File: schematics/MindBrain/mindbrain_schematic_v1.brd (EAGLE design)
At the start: 92.4 x 49.5 mm, 47 parts, among them CON1 POWER, IC1 TL084P, IC2 TL084P

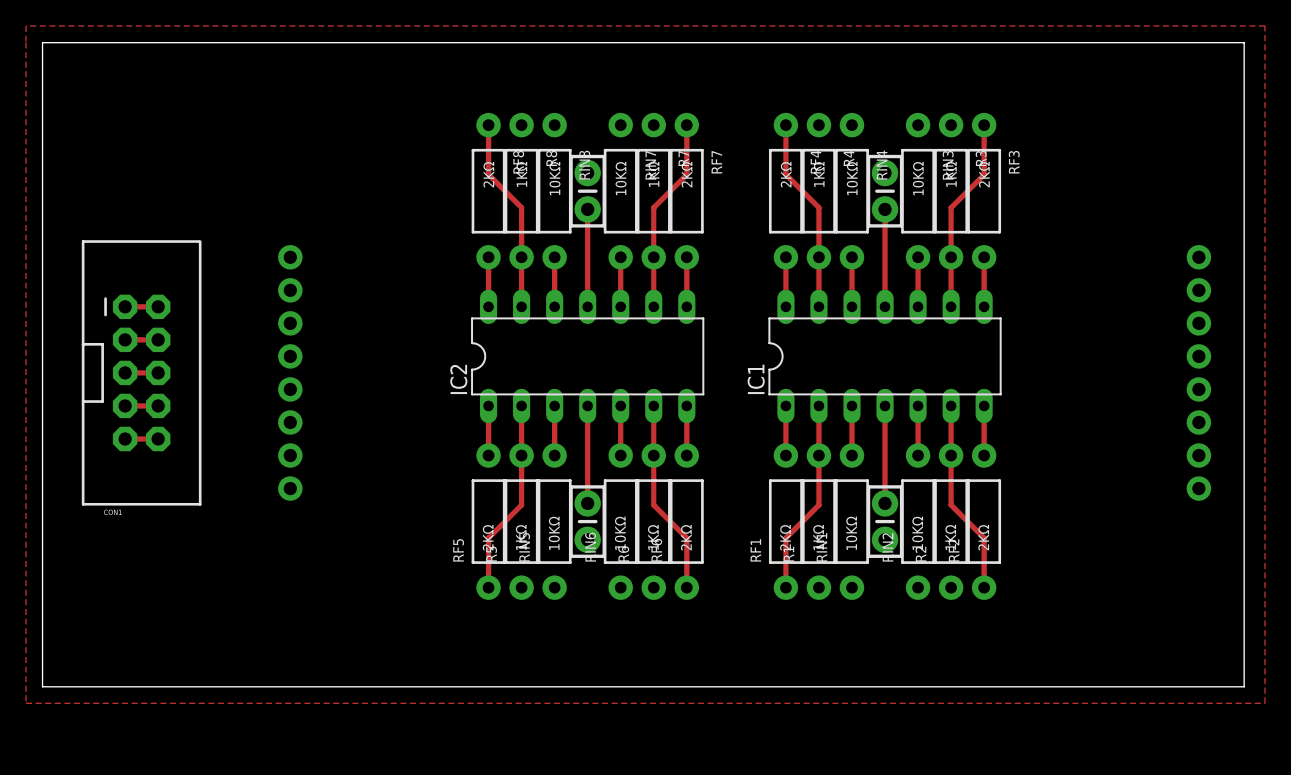
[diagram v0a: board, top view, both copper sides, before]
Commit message: not so sure about ground pour. Going back to airwired grounds for now
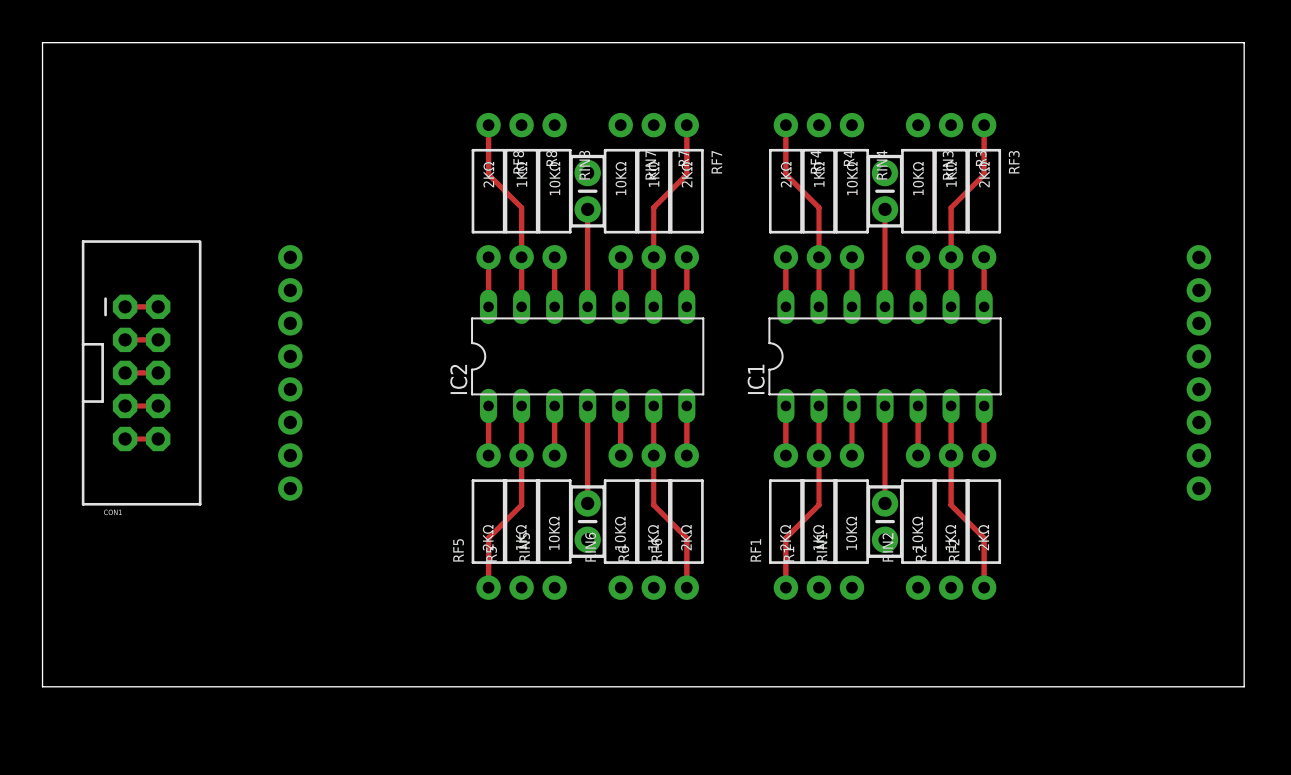
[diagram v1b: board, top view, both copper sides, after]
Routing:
- removed copper zone on layer 1, net GND
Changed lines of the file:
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@@
 <contactref element="RIN1" pad="P$2"/>
 <contactref element="IC1" pad="3"/>
+<wire x1="19.05" y1="15.24" x2="62.23" y2="17.78" width="0" layer="19" extent="1-1"/>
 <wire x1="62.23" y1="21.59" x2="62.23" y2="17.78" width="0.4064" layer="1"/>
-<wire x1="19.05" y1="15.24" x2="62.23" y2="17.78" width="0" layer="19" extent="1-1"/>
 </signal>
 <signal name="GND">
@@
 <wire x1="6.35" y1="26.67" x2="8.89" y2="26.67" width="0.4064" layer="1"/>
 <wire x1="6.35" y1="24.13" x2="8.89" y2="24.13" width="0.4064" layer="1"/>
-<polygon width="0.4064" layer="1">
-<vertex x="-1.27" y="-1.27"/>
-<vertex x="93.98" y="-1.27"/>
-<vertex x="93.98" y="50.8"/>
-<vertex x="-1.27" y="50.8"/>
-<vertex x="-1.27" y="49.53"/>
-</polygon>
+<wire x1="67.31" y1="43.18" x2="69.85" y2="43.18" width="0" layer="19" extent="1-1"/>
+<wire x1="64.77" y1="39.497" x2="67.31" y2="43.18" width="0" layer="19" extent="1-1"/>
+<wire x1="62.23" y1="43.18" x2="64.77" y2="39.497" width="0" layer="19" extent="1-1"/>
+<wire x1="59.69" y1="43.18" x2="62.23" y2="43.18" width="0" layer="19" extent="1-1"/>
+<wire x1="46.99" y1="43.18" x2="59.69" y2="43.18" width="0" layer="19" extent="1-1"/>
+<wire x1="44.45" y1="43.18" x2="46.99" y2="43.18" width="0" layer="19" extent="1-1"/>
+<wire x1="41.91" y1="39.497" x2="44.45" y2="43.18" width="0" layer="19" extent="1-1"/>
+<wire x1="39.37" y1="43.18" x2="41.91" y2="39.497" width="0" layer="19" extent="1-1"/>
+<wire x1="36.83" y1="43.18" x2="39.37" y2="43.18" width="0" layer="19" extent="1-1"/>
+<wire x1="64.77" y1="11.303" x2="64.77" y2="39.497" width="0" layer="19" extent="1-1"/>
+<wire x1="67.31" y1="7.62" x2="64.77" y2="11.303" width="0" layer="19" extent="1-1"/>
+<wire x1="69.85" y1="7.62" x2="67.31" y2="7.62" width="0" layer="19" extent="1-1"/>
+<wire x1="62.23" y1="7.62" x2="64.77" y2="11.303" width="0" layer="19" extent="1-1"/>
+<wire x1="59.69" y1="7.62" x2="62.23" y2="7.62" width="0" layer="19" extent="1-1"/>
+<wire x1="46.99" y1="7.62" x2="59.69" y2="7.62" width="0" layer="19" extent="1-1"/>
+<wire x1="44.45" y1="7.62" x2="46.99" y2="7.62" width="0" layer="19" extent="1-1"/>
+<wire x1="41.91" y1="11.303" x2="44.45" y2="7.62" width="0" layer="19" extent="1-1"/>
+<wire x1="39.37" y1="7.62" x2="41.91" y2="11.303" width="0" layer="19" extent="1-1"/>
+<wire x1="36.83" y1="7.62" x2="39.37" y2="7.62" width="0" layer="19" extent="1-1"/>
+<wire x1="8.89" y1="21.59" x2="36.83" y2="7.62" width="0" layer="19" extent="1-1"/>
+<wire x1="8.89" y1="24.13" x2="8.89" y2="21.59" width="0" layer="19" extent="1-1"/>
+<wire x1="8.89" y1="26.67" x2="8.89" y2="24.13" width="0" layer="19" extent="1-1"/>
 </signal>
 <signal name="N$2">
@@
 <contactref element="RF1" pad="P$2"/>
 <contactref element="IC1" pad="1"/>
+<wire x1="57.15" y1="17.78" x2="88.9" y2="15.24" width="0" layer="19" extent="1-1"/>
 <wire x1="57.15" y1="21.59" x2="57.15" y2="17.78" width="0.4064" layer="1"/>
-<wire x1="57.15" y1="17.78" x2="88.9" y2="15.24" width="0" layer="19" extent="1-1"/>
 </signal>
 <signal name="N$3">
@@
 <contactref element="RIN2" pad="P$2"/>
 <contactref element="IC1" pad="5"/>
+<wire x1="19.05" y1="17.78" x2="67.31" y2="17.78" width="0" layer="19" extent="1-1"/>
 <wire x1="67.31" y1="21.59" x2="67.31" y2="17.78" width="0.4064" layer="1"/>
-<wire x1="19.05" y1="17.78" x2="67.31" y2="17.78" width="0" layer="19" extent="1-1"/>
 </signal>
 <signal name="N$5">
@@
 <contactref element="IC1" pad="7"/>
 <wire x1="72.39" y1="21.59" x2="72.39" y2="17.78" width="0.4064" layer="1"/>
-<wire x1="72.39" y1="17.78" x2="88.9" y2="17.78" width="0" layer="19" extent="1-1"/>
+<wire x1="88.9" y1="17.78" x2="72.39" y2="17.78" width="0" layer="19" extent="1-16"/>
 </signal>
 <signal name="N$6">
@@
 <contactref element="RIN3" pad="P$2"/>
 <contactref element="IC1" pad="10"/>
+<wire x1="19.05" y1="20.32" x2="67.31" y2="33.02" width="0" layer="19" extent="1-1"/>
 <wire x1="67.31" y1="29.21" x2="67.31" y2="33.02" width="0.4064" layer="1"/>
-<wire x1="19.05" y1="20.32" x2="67.31" y2="29.21" width="0" layer="19" extent="1-1"/>
 </signal>
 <signal name="N$8">
@@
 <contactref element="IC1" pad="8"/>
 <wire x1="72.39" y1="29.21" x2="72.39" y2="33.02" width="0.4064" layer="1"/>
-<wire x1="72.39" y1="29.21" x2="88.9" y2="20.32" width="0" layer="19" extent="1-1"/>
+<wire x1="72.39" y1="33.02" x2="88.9" y2="20.32" width="0" layer="19" extent="1-16"/>
 </signal>
 <signal name="N$9">
@@
 <contactref element="RIN4" pad="P$2"/>
 <contactref element="IC1" pad="12"/>
+<wire x1="62.23" y1="33.02" x2="19.05" y2="22.86" width="0" layer="19" extent="1-1"/>
 <wire x1="62.23" y1="29.21" x2="62.23" y2="33.02" width="0.4064" layer="1"/>
-<wire x1="19.05" y1="22.86" x2="62.23" y2="29.21" width="0" layer="19" extent="1-1"/>
 </signal>
 <signal name="N$11">
@@
 <contactref element="RF4" pad="P$2"/>
 <contactref element="IC1" pad="14"/>
+<wire x1="57.15" y1="33.02" x2="88.9" y2="22.86" width="0" layer="19" extent="1-1"/>
 <wire x1="57.15" y1="29.21" x2="57.15" y2="33.02" width="0.4064" layer="1"/>
-<wire x1="57.15" y1="29.21" x2="88.9" y2="22.86" width="0" layer="19" extent="1-1"/>
 </signal>
 <signal name="N$12">
@@
 <contactref element="RIN5" pad="P$2"/>
 <contactref element="IC2" pad="3"/>
+<wire x1="19.05" y1="25.4" x2="39.37" y2="17.78" width="0" layer="19" extent="1-1"/>
 <wire x1="39.37" y1="21.59" x2="39.37" y2="17.78" width="0.4064" layer="1"/>
-<wire x1="19.05" y1="25.4" x2="39.37" y2="21.59" width="0" layer="19" extent="1-1"/>
 </signal>
 <signal name="N$14">
@@
 <contactref element="RF5" pad="P$2"/>
 <contactref element="IC2" pad="1"/>
+<wire x1="88.9" y1="25.4" x2="34.29" y2="17.78" width="0" layer="19" extent="1-1"/>
 <wire x1="34.29" y1="21.59" x2="34.29" y2="17.78" width="0.4064" layer="1"/>
-<wire x1="34.29" y1="21.59" x2="88.9" y2="25.4" width="0" layer="19" extent="1-1"/>
 </signal>
 <signal name="N$15">
@@
 <contactref element="RIN6" pad="P$2"/>
 <contactref element="IC2" pad="5"/>
+<wire x1="19.05" y1="27.94" x2="44.45" y2="17.78" width="0" layer="19" extent="1-1"/>
 <wire x1="44.45" y1="17.78" x2="44.45" y2="21.59" width="0.4064" layer="1"/>
-<wire x1="19.05" y1="27.94" x2="44.45" y2="21.59" width="0" layer="19" extent="1-1"/>
 </signal>
 <signal name="N$17">
@@
 <contactref element="RF6" pad="P$2"/>
 <contactref element="IC2" pad="7"/>
+<wire x1="88.9" y1="27.94" x2="49.53" y2="17.78" width="0" layer="19" extent="1-1"/>
 <wire x1="49.53" y1="21.59" x2="49.53" y2="17.78" width="0.4064" layer="1"/>
-<wire x1="49.53" y1="21.59" x2="88.9" y2="27.94" width="0" layer="19" extent="1-1"/>
 </signal>
 <signal name="N$18">
@@
 <contactref element="RIN7" pad="P$2"/>
 <contactref element="IC2" pad="10"/>
+<wire x1="44.45" y1="33.02" x2="19.05" y2="30.48" width="0" layer="19" extent="1-1"/>
 <wire x1="44.45" y1="33.02" x2="44.45" y2="29.21" width="0.4064" layer="1"/>
-<wire x1="19.05" y1="30.48" x2="44.45" y2="29.21" width="0" layer="19" extent="1-1"/>
 </signal>
 <signal name="N$20">
@@
 <contactref element="RF7" pad="P$2"/>
 <contactref element="IC2" pad="8"/>
+<wire x1="88.9" y1="30.48" x2="49.53" y2="33.02" width="0" layer="19" extent="1-1"/>
 <wire x1="49.53" y1="29.21" x2="49.53" y2="33.02" width="0.4064" layer="1"/>
-<wire x1="49.53" y1="29.21" x2="88.9" y2="30.48" width="0" layer="19" extent="1-1"/>
 </signal>
 <signal name="N$21">
@@
 <contactref element="RIN8" pad="P$2"/>
 <contactref element="IC2" pad="12"/>
+<wire x1="19.05" y1="33.02" x2="39.37" y2="33.02" width="0" layer="19" extent="1-1"/>
 <wire x1="39.37" y1="29.21" x2="39.37" y2="33.02" width="0.4064" layer="1"/>
-<wire x1="19.05" y1="33.02" x2="39.37" y2="33.02" width="0" layer="19" extent="1-1"/>
 </signal>
 <signal name="N$23">
@@
 <contactref element="C2" pad="1"/>
 <contactref element="C4" pad="1"/>
+<wire x1="41.91" y1="29.21" x2="64.77" y2="29.21" width="0" layer="19" extent="1-1"/>
 <wire x1="64.77" y1="36.703" x2="64.77" y2="29.21" width="0.4064" layer="1"/>
 <wire x1="41.91" y1="36.703" x2="41.91" y2="29.21" width="0.4064" layer="1"/>
+<wire x1="8.89" y1="29.21" x2="41.91" y2="29.21" width="0" layer="19" extent="1-1"/>
 <wire x1="6.35" y1="29.21" x2="8.89" y2="29.21" width="0.4064" layer="1"/>
-<wire x1="41.91" y1="36.703" x2="64.77" y2="36.703" width="0" layer="19" extent="1-1"/>
-<wire x1="8.89" y1="29.21" x2="41.91" y2="29.21" width="0" layer="19" extent="1-1"/>
 </signal>
 <signal name="N$25">
@@
 <contactref element="C3" pad="1"/>
 <contactref element="CON1" pad="10"/>
+<wire x1="41.91" y1="21.59" x2="64.77" y2="21.59" width="0" layer="19" extent="1-1"/>
+<wire x1="8.89" y1="19.05" x2="41.91" y2="21.59" width="0" layer="19" extent="1-1"/>
 <wire x1="64.77" y1="14.097" x2="64.77" y2="21.59" width="0.4064" layer="1"/>
 <wire x1="41.91" y1="14.097" x2="41.91" y2="21.59" width="0.4064" layer="1"/>
 <wire x1="6.35" y1="19.05" x2="8.89" y2="19.05" width="0.4064" layer="1"/>
-<wire x1="41.91" y1="21.59" x2="64.77" y2="21.59" width="0" layer="19" extent="1-1"/>
-<wire x1="8.89" y1="19.05" x2="41.91" y2="21.59" width="0" layer="19" extent="1-1"/>
 </signal>
 </signals>

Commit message: added audio input and output grounds
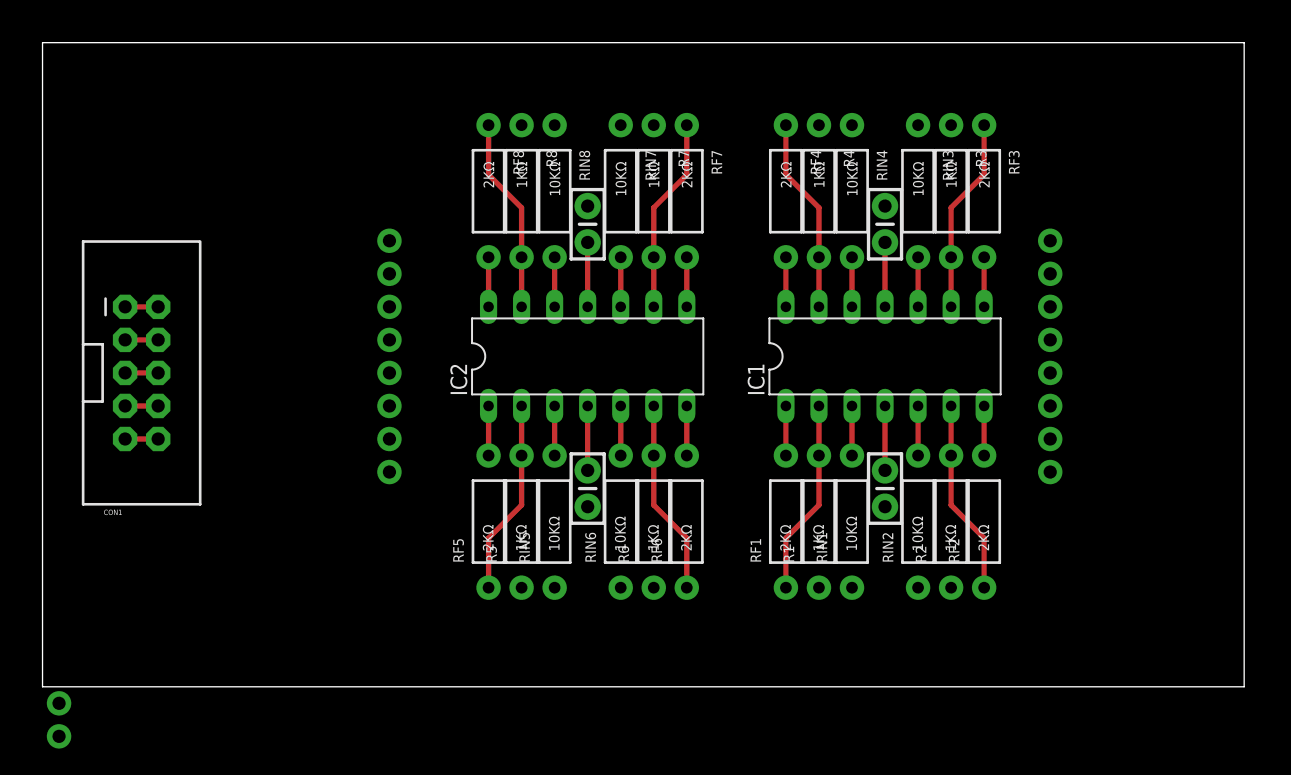
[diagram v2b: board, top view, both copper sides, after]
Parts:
- added AUDIOCARD-GND, OUTPUT-GND: (no value), SparkFun-Connectors:1X01NS-KIT
- moved OUTPUT1 11.5 mm to (77.5, 16.5)
- moved OUTPUT2 11.5 mm to (77.5, 19.1)
- moved OUTPUT3 11.5 mm to (77.5, 21.6)
- moved OUTPUT4 11.5 mm to (77.5, 24.1)
- moved OUTPUT5 11.5 mm to (77.5, 26.7)
- moved OUTPUT6 11.5 mm to (77.5, 29.2)
- moved OUTPUT7 11.5 mm to (77.5, 31.8)
- moved OUTPUT8 11.5 mm to (77.5, 34.3)
- moved INPUT1 7.73 mm to (26.7, 16.5)
- moved INPUT5 7.73 mm to (26.7, 26.7), turned to 90 degrees
- moved INPUT2 7.73 mm to (26.7, 19.1)
- moved INPUT3 7.73 mm to (26.7, 21.6)
- moved INPUT4 7.73 mm to (26.7, 24.1)
- moved INPUT6 7.73 mm to (26.7, 29.2)
- moved INPUT7 7.73 mm to (26.7, 31.8)
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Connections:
- net GND: now also AUDIOCARD-GND.1, OUTPUT-GND.1
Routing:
- net N$27: track 17.5 -> 12.4 mm
- net N$25: track 17.5 -> 12.4 mm

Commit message: trying new style board layout, flippinng orientation of feedback and input resistors
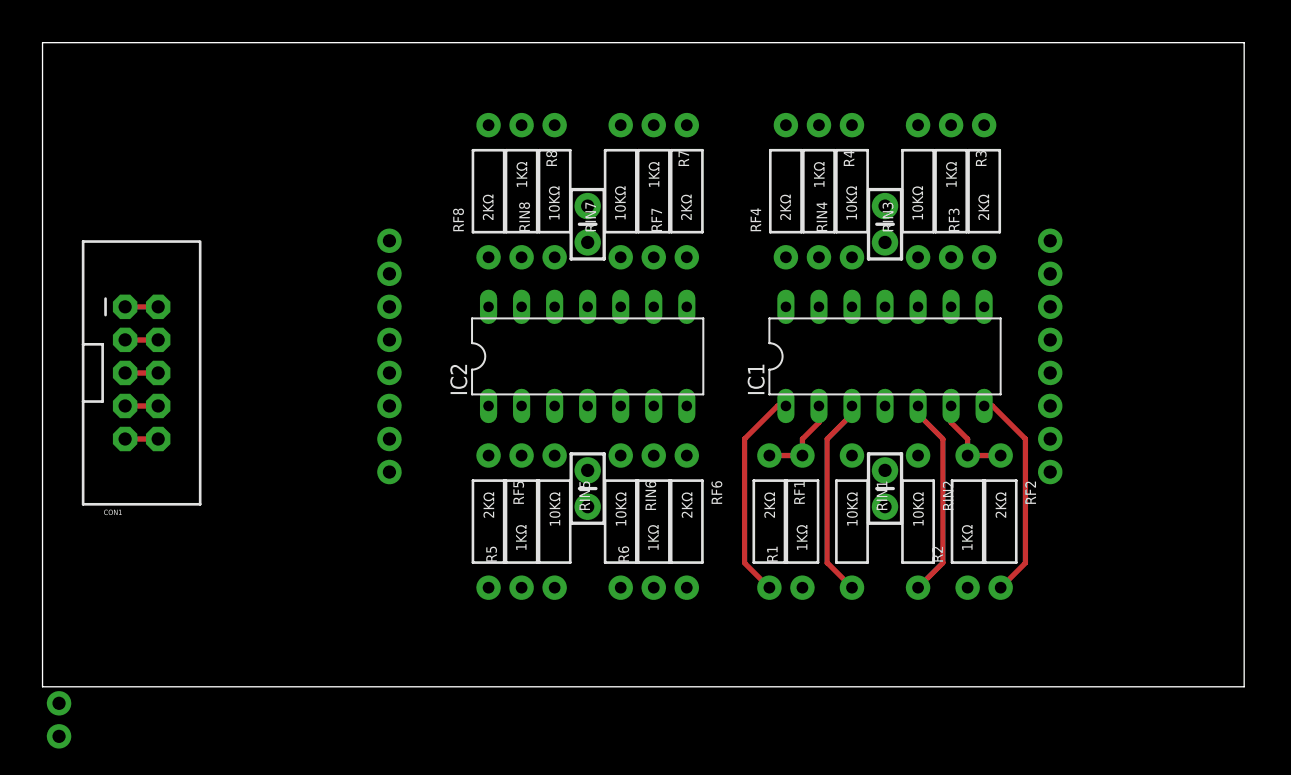
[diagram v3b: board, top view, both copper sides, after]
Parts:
- moved R2 1.27 mm to (71.1, 12.7)
- moved R1 1.27 mm to (58.4, 12.7)
- moved RF1 1.27 mm to (55.9, 12.7), turned to 270 degrees
- moved RF2 1.27 mm to (73.7, 12.7), turned to 270 degrees
- turned INPUT8 to 90 degrees
- turned RF3 to 90 degrees
- turned RF4 to 90 degrees
- turned RF5 to 270 degrees
- turned RF6 to 270 degrees
- turned RF7 to 90 degrees
- turned RF8 to 90 degrees
- turned RIN1 to 270 degrees
- turned RIN2 to 270 degrees
- turned RIN3 to 90 degrees
- turned RIN4 to 90 degrees
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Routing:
- net N$9: track 15.0 -> 0.00 mm
- net N$24: track 15.0 -> 0.00 mm
- net N$21: track 15.0 -> 0.00 mm
- net N$18: track 15.0 -> 0.00 mm
- net N$15: track 15.0 -> 0.00 mm
- net N$12: track 15.0 -> 0.00 mm
- net N$5: track 3.81 -> 16.4 mm
- net N$2: track 3.81 -> 16.4 mm
- net N$4: track 3.81 -> 15.5 mm
- net N$1: track 3.81 -> 15.5 mm
- net N$25: track 12.4 -> 2.54 mm
- net N$27: track 12.4 -> 2.54 mm
- net N$6: track 15.0 -> 6.88 mm
- net N$3: track 15.0 -> 6.88 mm
- net N$8: track 3.81 -> 0.00 mm
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
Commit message: layed out non io/pwr/gnd traces
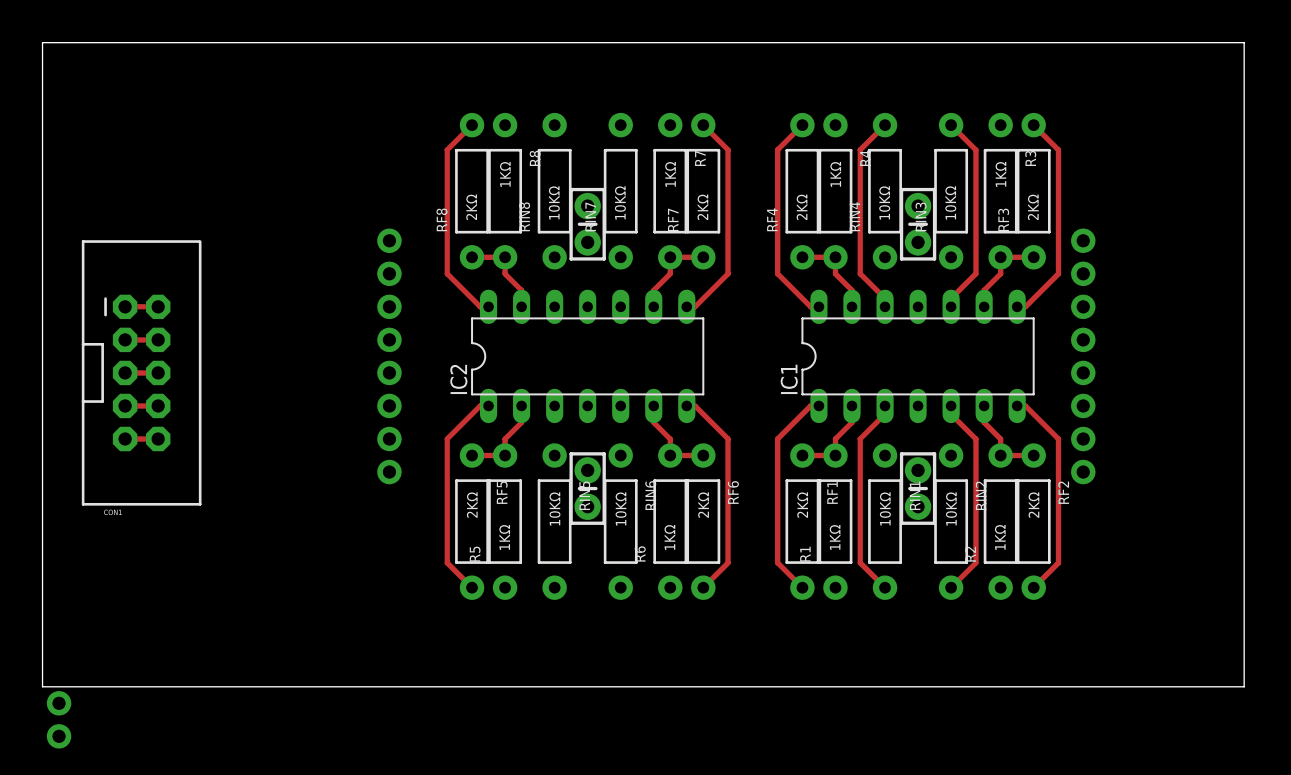
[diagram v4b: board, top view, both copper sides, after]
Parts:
- moved R3 3.81 mm to (73.7, 38.1)
- moved RF3 3.81 mm to (76.2, 38.1)
- moved C2 2.54 mm to (67.3, 35.6)
- moved C3 2.54 mm to (67.3, 15.2)
- moved IC1 2.54 mm to (67.3, 25.4)
- moved OUTPUT1 2.54 mm to (80.0, 16.5)
- moved OUTPUT2 2.54 mm to (80.0, 19.1)
- moved OUTPUT3 2.54 mm to (80.0, 21.6)
- moved OUTPUT4 2.54 mm to (80.0, 24.1)
- moved OUTPUT5 2.54 mm to (80.0, 26.7)
- moved OUTPUT6 2.54 mm to (80.0, 29.2)
- moved OUTPUT7 2.54 mm to (80.0, 31.8)
- moved OUTPUT8 2.54 mm to (80.0, 34.3)
- moved RF2 2.54 mm to (76.2, 12.7)
- moved R1 2.54 mm to (61.0, 12.7)
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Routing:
- net N$23: track 0.00 -> 16.4 mm
- net N$14: track 0.00 -> 16.4 mm
- net N$8: track 0.00 -> 16.4 mm
- net N$20: track 0.00 -> 16.4 mm
- net N$17: track 0.00 -> 16.4 mm
- net N$11: track 0.00 -> 16.4 mm
- net N$7: track 0.00 -> 15.5 mm
- net N$10: track 0.00 -> 15.5 mm
- net N$9: track 0.00 -> 6.88 mm
- net N$24: track 0.00 -> 6.88 mm
- net N$21: track 0.00 -> 6.88 mm
- net N$12: track 0.00 -> 6.88 mm
- net N$18: track 0.00 -> 6.88 mm
- net N$15: track 0.00 -> 6.88 mm
